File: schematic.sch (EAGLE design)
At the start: 125 parts, among them IC1 AD8015, IC2 AD8015, IC3 AD8015, IC4 AD8015

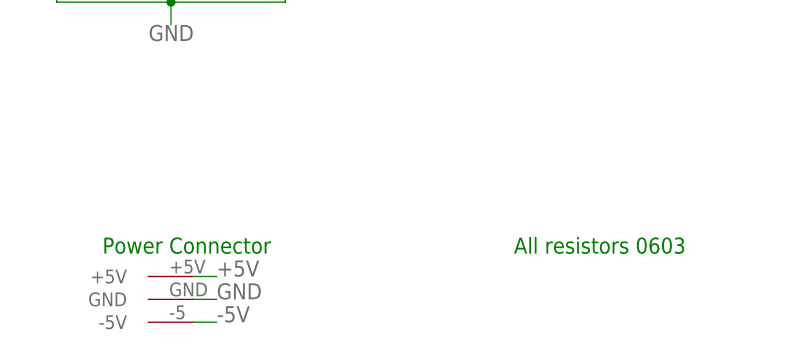
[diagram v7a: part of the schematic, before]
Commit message: Added second power plug
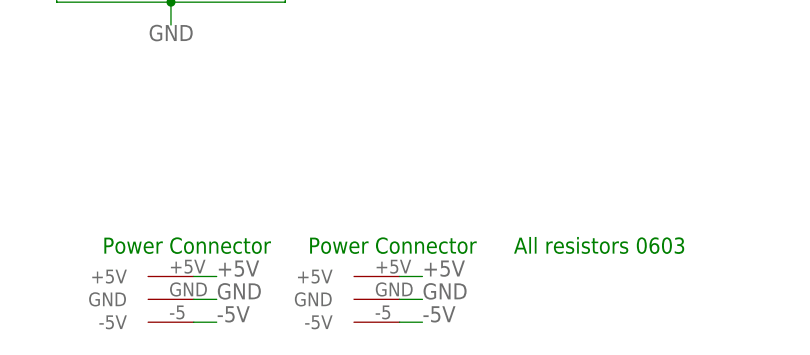
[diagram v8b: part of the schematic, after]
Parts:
- added U$22: DIVERSITYPWR, 12-ChannelEMG:DIVERSITYPWR
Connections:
- net +5V: now also U$22.+5V
- net -5V: now also U$22.-5V
- net GND: now also U$22.GND
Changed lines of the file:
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@@
 <part name="C63" library="rcl" deviceset="C-US" device="C1206" value="6.8uF"/>
 <part name="C64" library="rcl" deviceset="C-US" device="C1206" value="6.8uF"/>
+<part name="U$22" library="12-ChannelEMG" deviceset="DIVERSITYPWR" device=""/>
 </parts>
 <sheets>
@@
 <text x="385.318" y="110.744" size="1.778" layer="91" rot="R90">1206</text>
 <text x="385.318" y="87.884" size="1.778" layer="91" rot="R90">1206</text>
+<text x="132.08" y="-7.62" size="1.778" layer="91">Power Connector</text>
 </plain>
 <instances>
@@
 <attribute name="VALUE" x="387.731" y="89.916" size="1.778" layer="96" rot="R90"/>
 </instance>
+<instance part="U$22" gate="G$1" x="137.16" y="-12.7" rot="R180"/>
 </instances>
 <busses>
@@
 <junction x="492.76" y="35.56"/>
 <junction x="492.76" y="33.02"/>
+</segment>
+<segment>
+<pinref part="U$22" gate="G$1" pin="GND"/>
+<wire x1="142.24" y1="-12.7" x2="144.78" y2="-12.7" width="0.1524" layer="91"/>
+<label x="144.78" y="-12.7" size="1.778" layer="95"/>
 </segment>
 </net>
@@
 <label x="375.92" y="93.98" size="1.778" layer="95" rot="R90"/>
 <junction x="375.92" y="96.52"/>
+</segment>
+<segment>
+<pinref part="U$22" gate="G$1" pin="-5V"/>
+<wire x1="142.24" y1="-15.24" x2="144.78" y2="-15.24" width="0.1524" layer="91"/>
+<label x="144.78" y="-15.24" size="1.778" layer="95"/>
 </segment>
 </net>
@@
 <junction x="375.92" y="106.68"/>
 </segment>
+<segment>
+<pinref part="U$22" gate="G$1" pin="+5V"/>
+<wire x1="142.24" y1="-10.16" x2="144.78" y2="-10.16" width="0.1524" layer="91"/>
+<label x="144.78" y="-10.16" size="1.778" layer="95"/>
+</segment>
 </net>
